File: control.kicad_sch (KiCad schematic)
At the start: 24 parts, among them J4 Conn_01x05_Pin, J5 Conn_01x03_Pin, J6 Conn_01x03_Pin, Q4 DTC143Z, U6 STM32G031G8Ux

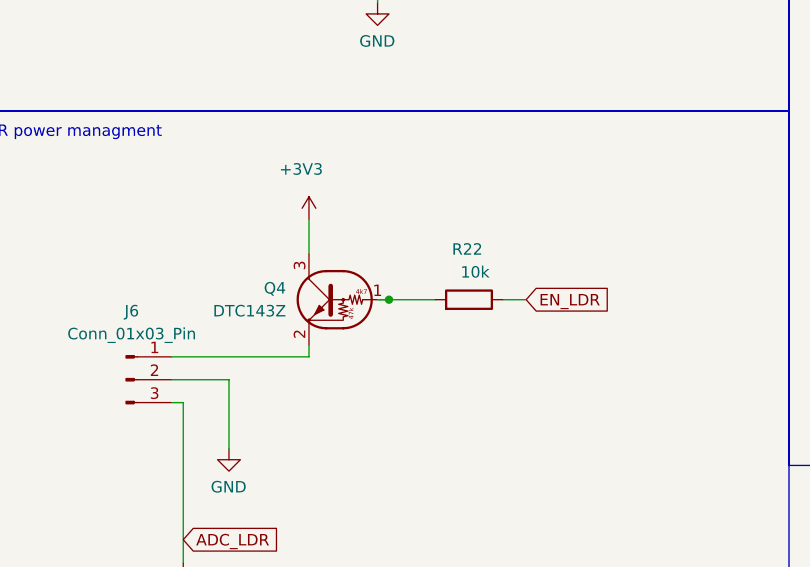
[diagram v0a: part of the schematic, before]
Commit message: Buffed MOSFETs - Changed Q1,Q2 to AO3400 - Changed Q4 to DMG1012T
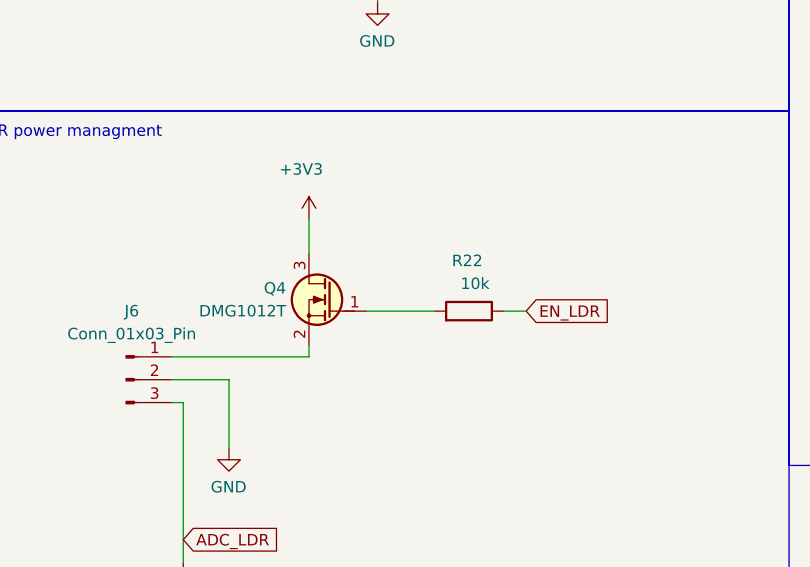
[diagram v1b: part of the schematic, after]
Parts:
- Q4: value DTC143Z -> DMG1012T; symbol Transistor_BJT:DTC143Z -> PCM_Transistor_MOSFET_AKL:DMG1012T; LCSC C6423741 -> C20512
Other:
- moved on the sheet: R22
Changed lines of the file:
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@@
-	)
-	(junction
-		(at 85.09 143.51)
-		(diameter 0)
-		(color 0 0 0 0)
 	)
 	(junction
@@
 	(wire
 		(pts
-			(xy 83.82 143.51) (xy 85.09 143.51)
-		)
-		(stroke
-			(width 0)
-			(type default)
-		)
-	)
-	(wire
-		(pts
 			(xy 160.02 46.99) (xy 144.78 46.99)
 		)
@@
 	(wire
 		(pts
-			(xy 97.79 143.51) (xy 100.33 143.51)
+			(xy 97.79 144.78) (xy 100.33 144.78)
 		)
 		(stroke
@@
 	(wire
 		(pts
-			(xy 85.09 143.51) (xy 90.17 143.51)
-		)
-		(stroke
-			(width 0)
-			(type default)
-		)
-	)
-	(wire
-		(pts
 			(xy 64.77 81.28) (xy 66.04 81.28)
 		)
@@
 		(pts
 			(xy 40.64 71.12) (xy 40.64 73.66)
+		)
+		(stroke
+			(width 0)
+			(type default)
+		)
+	)
+	(wire
+		(pts
+			(xy 82.55 144.78) (xy 90.17 144.78)
 		)
 		(stroke
@@
 	(global_label "EN_LDR"
 		(shape input)
-		(at 100.33 143.51 0)
+		(at 100.33 144.78 0)
 		(fields_autoplaced yes)
 		(effects
@@
 		)
 		(property "Intersheetrefs" "${INTERSHEET_REFS}"
-			(at 110.3304 143.51 0)
+			(at 110.3304 144.78 0)
 			(effects
 				(font
@@
 	)
 	(symbol
-		(lib_id "Transistor_BJT:DTC143Z")
+		(lib_id "PCM_Transistor_MOSFET_AKL:DMG1012T")
 		(at 78.74 143.51 0)
 		(mirror y)
@@
 			)
 		)
-		(property "Value" "DTC143Z"
-			(at 73.66 144.7799 0)
+		(property "Value" "DMG1012T"
+			(at 73.66 144.78 0)
 			(effects
 				(font
@@
 		)
 		(property "Footprint" "SOT-523:SOT-523"
+			(at 73.66 140.97 0)
+			(effects
+				(font
+					(size 1.27 1.27)
+				)
+				(hide yes)
+			)
+		)
+		(property "Datasheet" "https://www.tme.eu/Document/41ce6a9ee591bb7bae22a8b9f76bcbce/DMG1012T-DTE.pdf"
 			(at 78.74 143.51 0)
 			(effects
@@
 					(size 1.27 1.27)
 				)
-				(justify left)
-				(hide yes)
-			)
-		)
-		(property "Datasheet" ""
+				(hide yes)
+			)
+		)
+		(property "Description" "SOT-523 N-MOSFET enchancement mode transistor, 20V, 630mA, 280mW, Alternate KiCAD Library"
 			(at 78.74 143.51 0)
 			(effects
@@
 					(size 1.27 1.27)
 				)
-				(justify left)
-				(hide yes)
-			)
-		)
-		(property "Description" "Digital NPN Transistor, 4k7/47k, SOT-23"
-			(at 78.74 143.51 0)
-			(effects
-				(font
-					(size 1.27 1.27)
-				)
-				(hide yes)
-			)
-		)
-		(property "LCSC" "C6423741"
+				(hide yes)
+			)
+		)
+		(property "LCSC" "C20512"
 			(at 78.74 143.51 0)
 			(effects
@@
 	(symbol
 		(lib_id "Device:R")
-		(at 93.98 143.51 270)
+		(at 93.98 144.78 270)
 		(mirror x)
 		(unit 1)
@@
 		(dnp no)
 		(property "Reference" "R22"
-			(at 95.504 137.922 90)
+			(at 95.504 139.192 90)
 			(effects
 				(font
@@
 		)
 		(property "Value" "10k"
-			(at 96.266 140.462 90)
+			(at 96.266 141.732 90)
 			(effects
 				(font
@@
 		)
 		(property "Footprint" "Resistor_SMD:R_0603_1608Metric"
-			(at 93.98 145.288 90)
+			(at 93.98 146.558 90)
 			(effects
 				(font
@@
 		)
 		(property "Datasheet" "~"
-			(at 93.98 143.51 0)
+			(at 93.98 144.78 0)
 			(effects
 				(font
@@
 		)
 		(property "Description" "Resistor"
-			(at 93.98 143.51 0)
+			(at 93.98 144.78 0)
 			(effects
 				(font
@@
 		)
 		(property "lcsc" ""
-			(at 93.98 143.51 0)
-			(effects
-				(font
+			(at 93.98 144.78 0)
+			(effects
+				(font

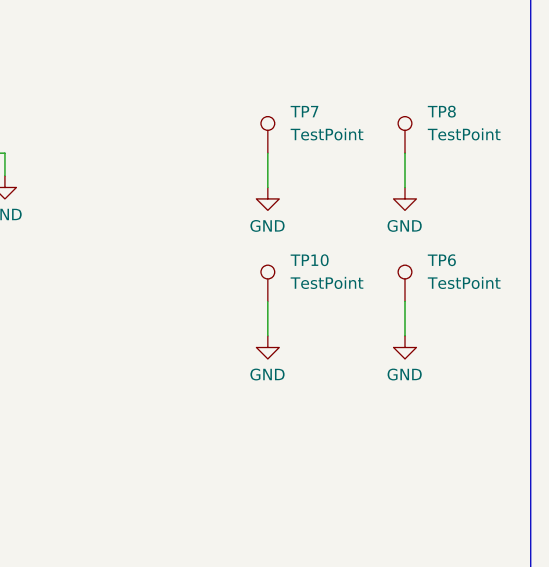
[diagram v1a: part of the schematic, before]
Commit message: Adjusted stencil for custom jig
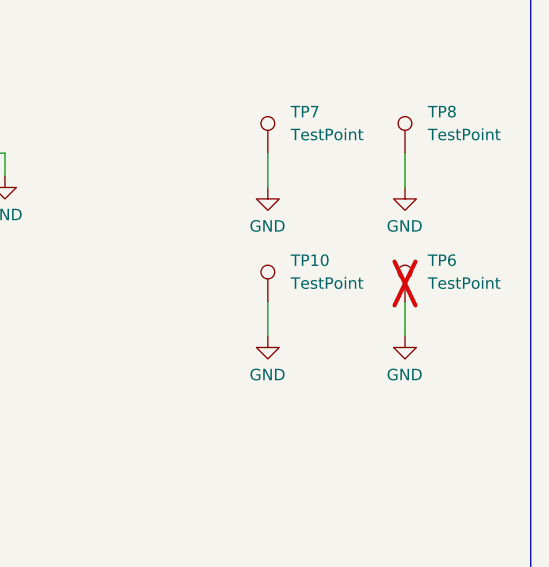
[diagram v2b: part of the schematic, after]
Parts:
- TP6: now not fitted
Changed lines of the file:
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@@
 		(in_bom no)
 		(on_board yes)
-		(dnp no)
+		(dnp yes)
 		(fields_autoplaced yes)
 		(property "Reference" "TP6"

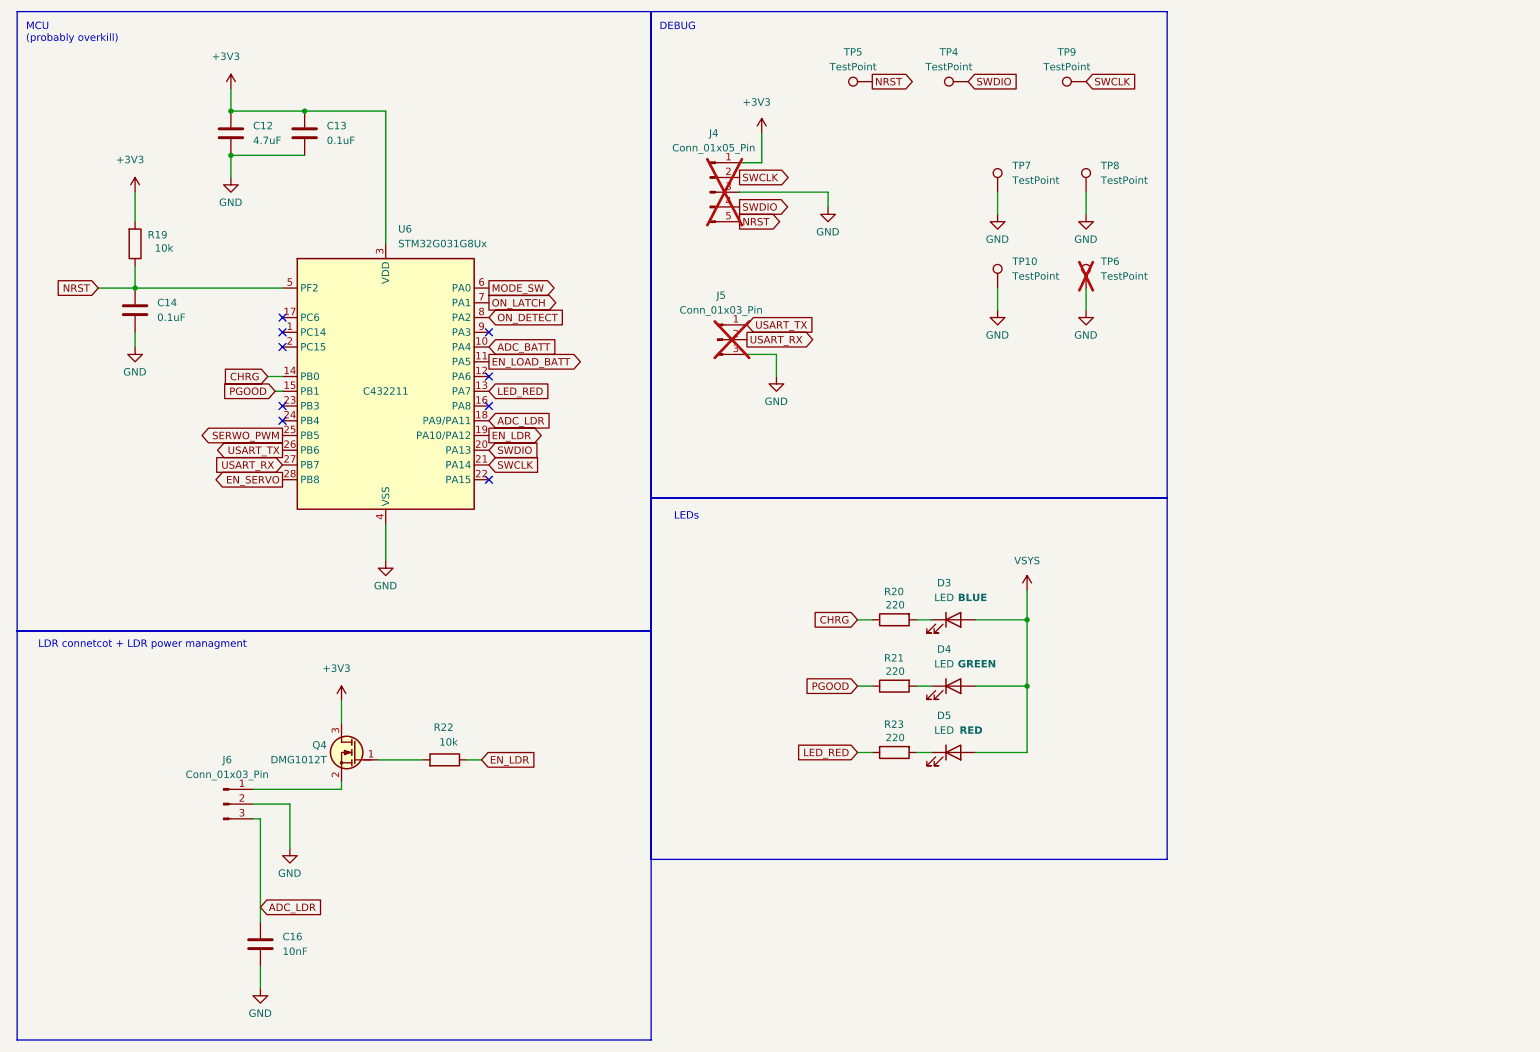
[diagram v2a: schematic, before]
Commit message: Rough placment of components for v3
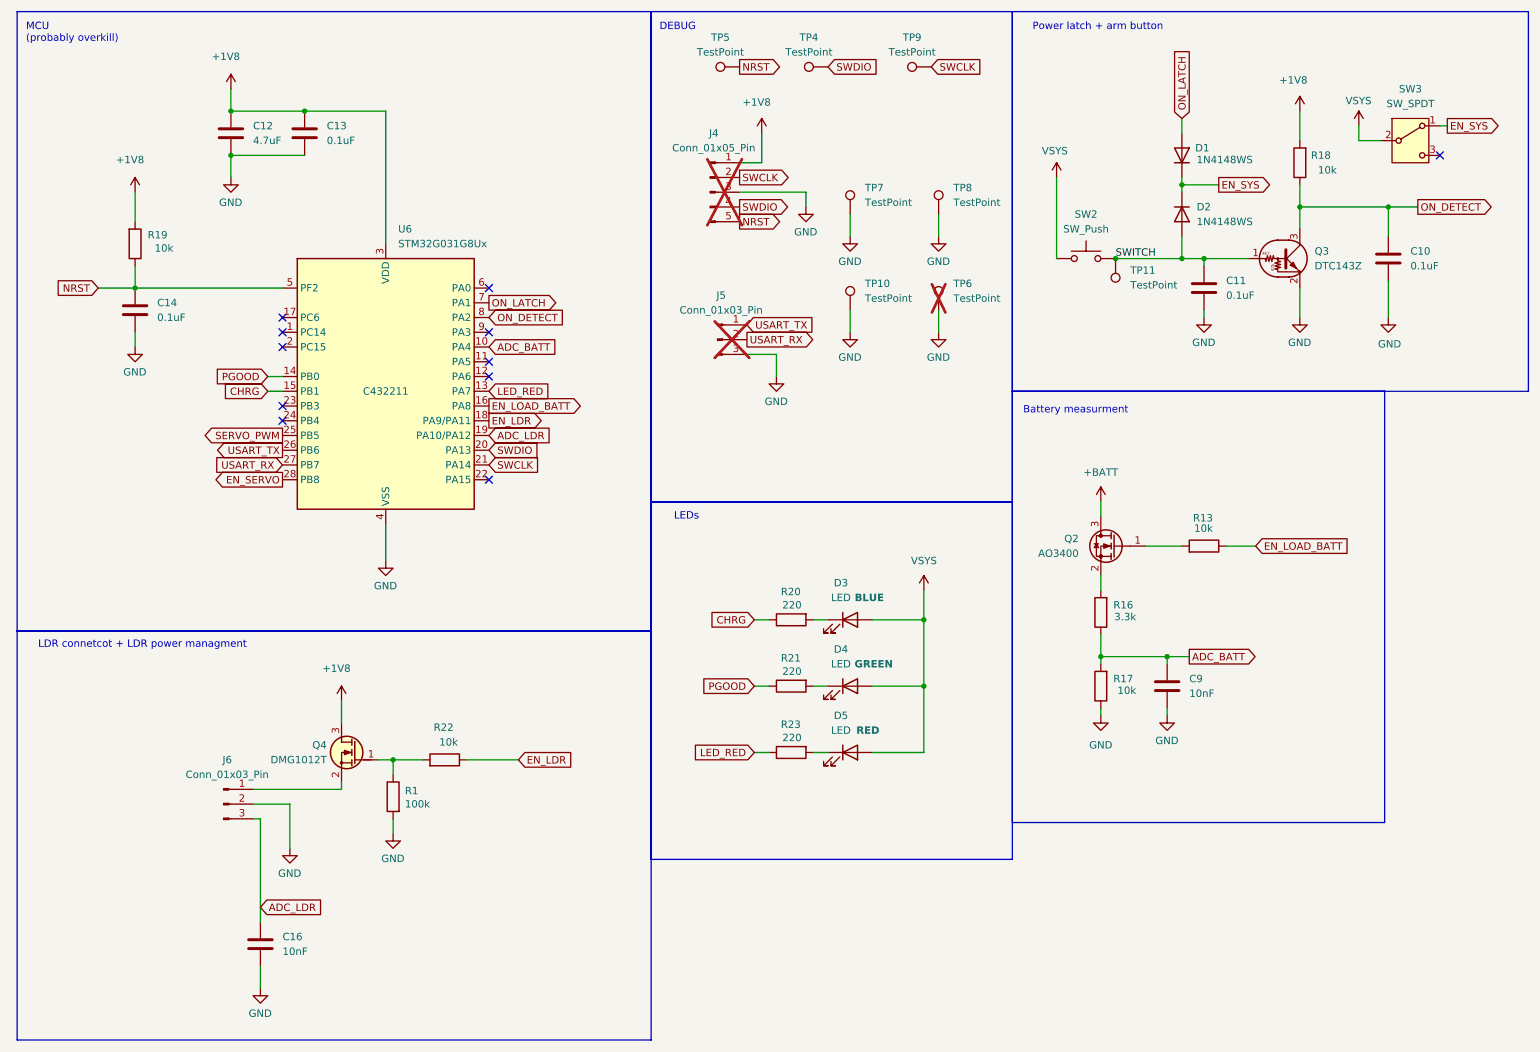
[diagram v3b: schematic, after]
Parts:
- added C10, C11: 0.1uF, Capacitor_SMD:C_0603_1608Metric, symbol Device:C
- added C9: 10nF, Capacitor_SMD:C_0603_1608Metric, symbol Device:C
- added D1, D2: 1N4148WS, Diode_SMD:D_SOD-323, symbol Diode:1N4148WS
- added Q2: AO3400, Package_TO_SOT_SMD:SOT-23, symbol Transistor_FET:AO3400A
- added Q3: DTC143Z, SOT-523:SOT-523, symbol Transistor_BJT:DTC143Z
- added R1: 100k, Resistor_SMD:R_0603_1608Metric, symbol Device:R
- added R13, R17, R18: 10k, Resistor_SMD:R_0603_1608Metric, symbol Device:R
- added R16: 3.3k, Resistor_SMD:R_0603_1608Metric, symbol Device:R
- added SW2: SW_Push, Button_Switch_THT:SW_Tactile_SPST_Angled_PTS645Vx58-2LFS, symbol Switch:SW_Push
- added SW3: SW_SPDT, Button_Switch_THT:SW_Slide_SPDT_Angled_CK_OS102011MA1Q, symbol Switch:SW_SPDT
- added TP11: TestPoint, TestPoint:TestPoint_Pad_D1.0mm, symbol Connector:TestPoint
- Q4: footprint SOT-523:SOT-523 -> Muffin_SMD:SOT-523
- U6: footprint STM32G031G8Ux:QFN-28_4x4mm_P0.5mm -> Muffin_SMD:QFN-28_4x4mm_P0.5mm
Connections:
- net ADC_BATT: now also C9.1, R16.1, R17.2
- net ADC_LDR: now also U6.19 (PA10/PA12); no longer U6.18 (PA9/PA11)
- net CHRG: now also U6.15 (PB1); no longer U6.14 (PB0)
- net EN_LDR: now also U6.18 (PA9/PA11); no longer U6.19 (PA10/PA12)
- net EN_LOAD_BATT: now also U6.16 (PA8), R13.1; no longer U6.11 (PA5)
- net GND: now also C10.2, C11.2, C9.2, Q3.2 (E), R1.2, R17.1
- net ON_DETECT: now also C10.1, Q3.3 (C), R18.1
- net ON_LATCH: now also D1.2 (A)
- net PGOOD: now also U6.14 (PB0); no longer U6.15 (PB1)
- net VSYS: now also SW2.1, SW3.2 (B)
- net at Q4.1 (G), R22.2: now also R1.1
- net +3V3 renamed +1V8
- net +1V8: now also R18.2
- net MODE_SW: no longer names the net of U6.6 (PA0)
- net SERWO_PWM renamed SERVO_PWM
- new net: Q2.2 (S), R16.2
- new net: Q2.1 (G), R13.2
- new net +BATT: Q2.3 (D)
- new net EN_SYS: D1.1 (K), D2.1 (K), SW3.1 (A)
- new net SWITCH: C11.1, D2.2 (A), Q3.1 (B), SW2.2, TP11.1
- no-connect marks 9 -> 11
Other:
- note added: "Battery measurment"
- note added: "Power latch + arm button"
- moved on the sheet: D3, D4, D5, R20, R21, R23, TP10, TP4, TP5, TP6, TP7, TP8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

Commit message: Routed v3
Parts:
- removed TP10: TestPoint, TestPoint:TestPoint_Pad_D1.0mm, symbol Connector:TestPoint
- added TP1, TP2: TestPoint, TestPoint:TestPoint_Pad_D1.0mm, symbol Connector:TestPoint
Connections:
- net CHRG: now also D3.1 (K); no longer R20.1
- net LED_RED: now also D5.1 (K); no longer R23.1
- net PGOOD: now also D4.1 (K); no longer R21.1
- net USART_RX: now also TP2.1
- net USART_TX: now also TP1.1
- net VSYS: now also R20.2, R21.2, R23.2; no longer D3.2 (A), D4.2 (A), D5.2 (A)
- new net: D5.2 (A), R23.1
- new net: D3.2 (A), R20.1
- new net: D4.2 (A), R21.1
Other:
- moved on the sheet: D3, D4, D5, R20, R21, R23

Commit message: Finished v3
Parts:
- J6: footprint conn:PinHeader_1x03_P1.27mm_Vertical -> Muffin_CONNECTOR_THT:Connector_JST_1x03_P1.27mm
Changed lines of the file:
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@@
 		(on_board yes)
 		(dnp no)
-		(fields_autoplaced yes)
 		(property "Reference" "J6"
 			(at 56.515 144.78 0)
@@
 			)
 		)
-		(property "Footprint" "conn:PinHeader_1x03_P1.27mm_Vertical"
-			(at 55.88 152.4 0)
+		(property "Footprint" "Muffin_CONNECTOR_THT:Connector_JST_1x03_P1.27mm"
+			(at 56.896 163.068 0)
 			(effects
 				(font
 					(size 1.27 1.27)
 				)
-				(hide yes)
 			)
 		)

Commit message: Added stencil outline
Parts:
- TP6: footprint Connector_PinHeader_2.54mm:PinHeader_1x01_P2.54mm_Vertical -> TestPoint:TestPoint_Plated_Hole_D2.0mm
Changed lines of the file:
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@@
 			)
 		)
-		(property "Footprint" "Connector_PinHeader_2.54mm:PinHeader_1x01_P2.54mm_Vertical"
+		(property "Footprint" "TestPoint:TestPoint_Plated_Hole_D2.0mm"
 			(at 184.15 67.31 0)
 			(effects

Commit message: Expanded documentation
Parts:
- added R8: 100k, Resistor_SMD:R_0603_1608Metric, symbol Device:R
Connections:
- net GND: now also R8.2
- net at Q2.1 (G), R13.2: now also R8.1
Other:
- moved on the sheet: C9, R16, R17

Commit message: Updated schematics. Calculated inductor values
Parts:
- SW3: LCSC (none) -> C398057
